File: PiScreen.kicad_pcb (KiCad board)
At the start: 2 copper layers, 56 x 36.5 mm, 111 parts, among them P1 M02X05, P2 M02X05, P3 CONN_14, P4 CONN_5, P5 CONN_5, P6 CONN_5

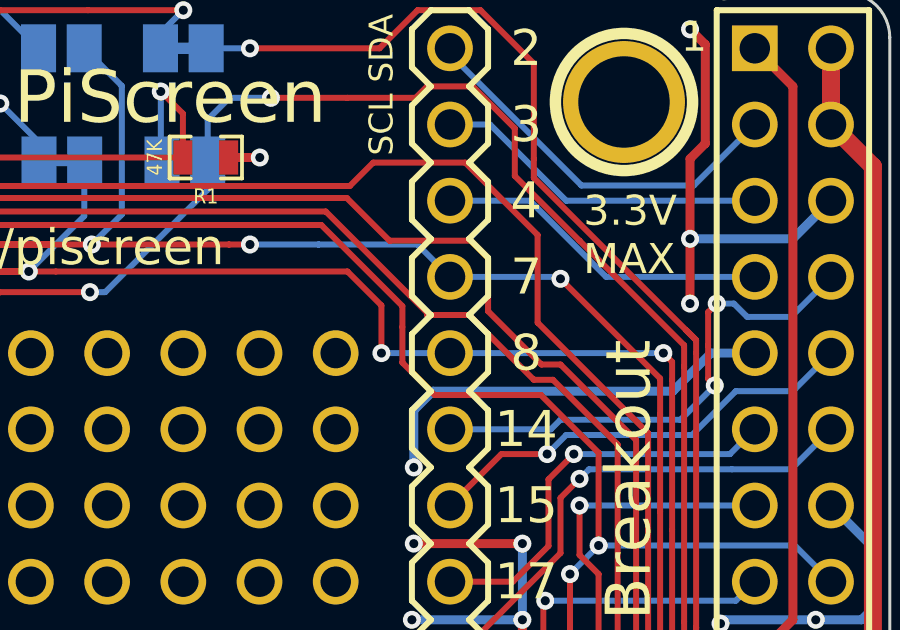
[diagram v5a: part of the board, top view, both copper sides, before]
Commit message: Mark CE0/CE1 pins as 'in use' on silkscreen, bump version to 1.2
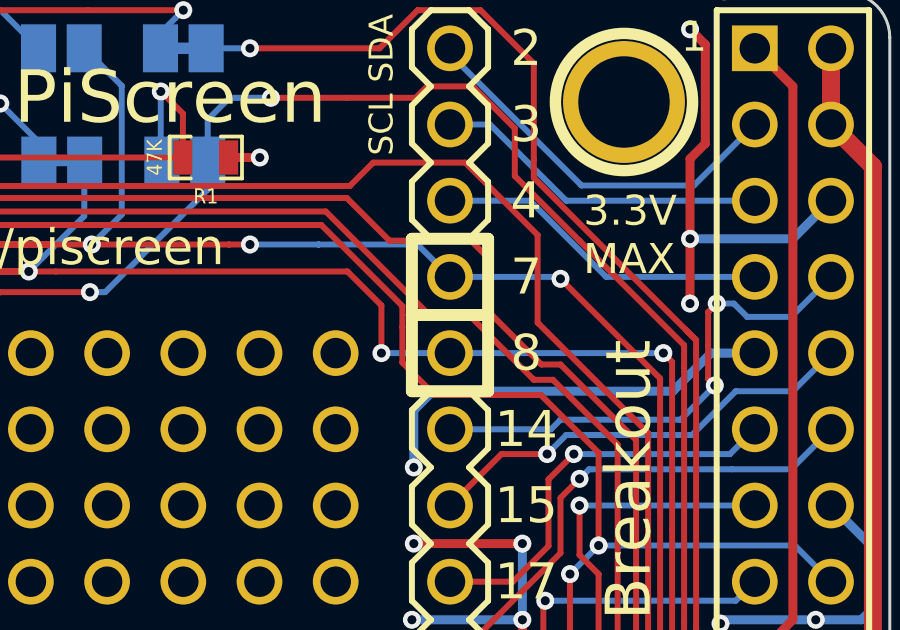
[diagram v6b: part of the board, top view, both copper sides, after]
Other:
- board text added: "V1.2 SKU: PISC"
- board text removed: "V1.1 SKU: PISC"
